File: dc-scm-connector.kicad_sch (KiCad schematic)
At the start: 10 parts, among them J19 Socket_Amphenol_ME10168134011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

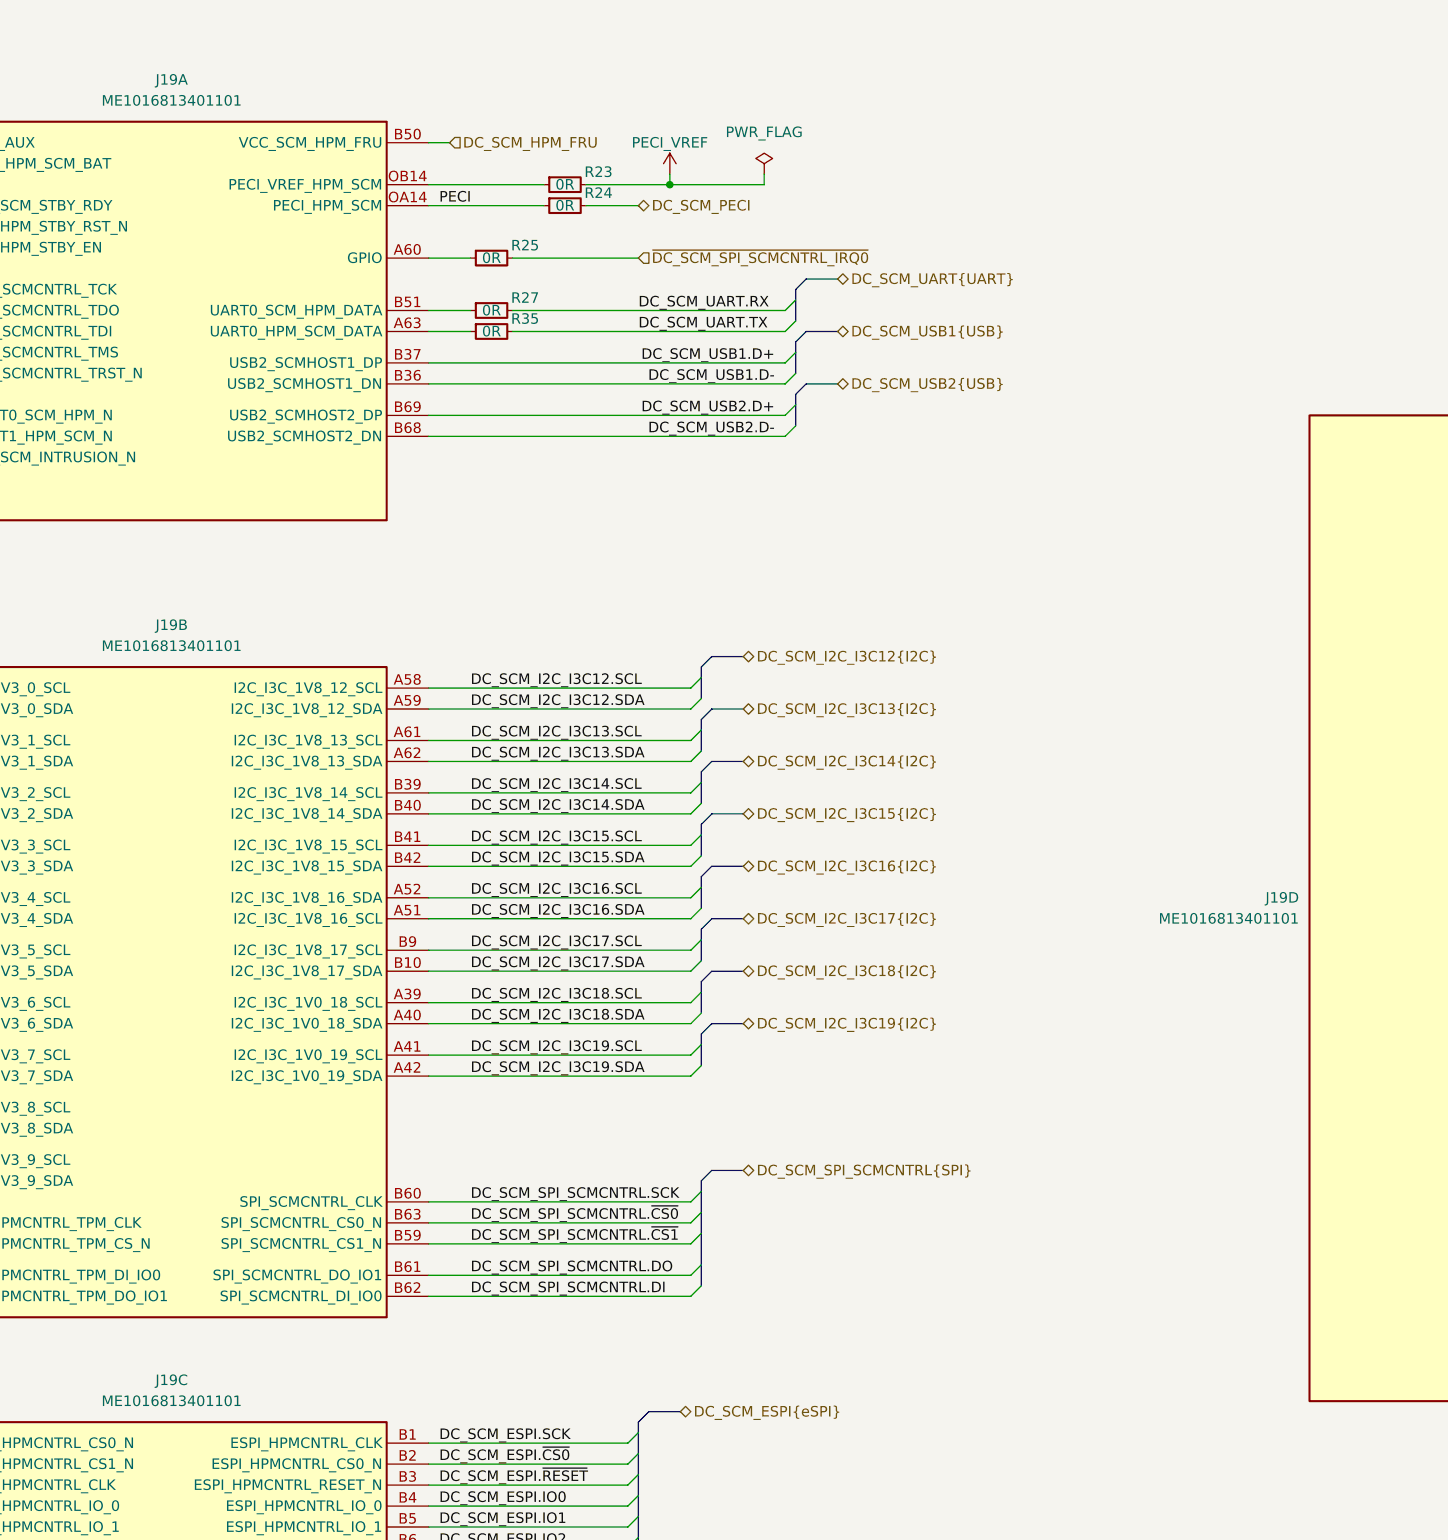
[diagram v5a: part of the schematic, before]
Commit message: [#92504] Update Annotation for connectors
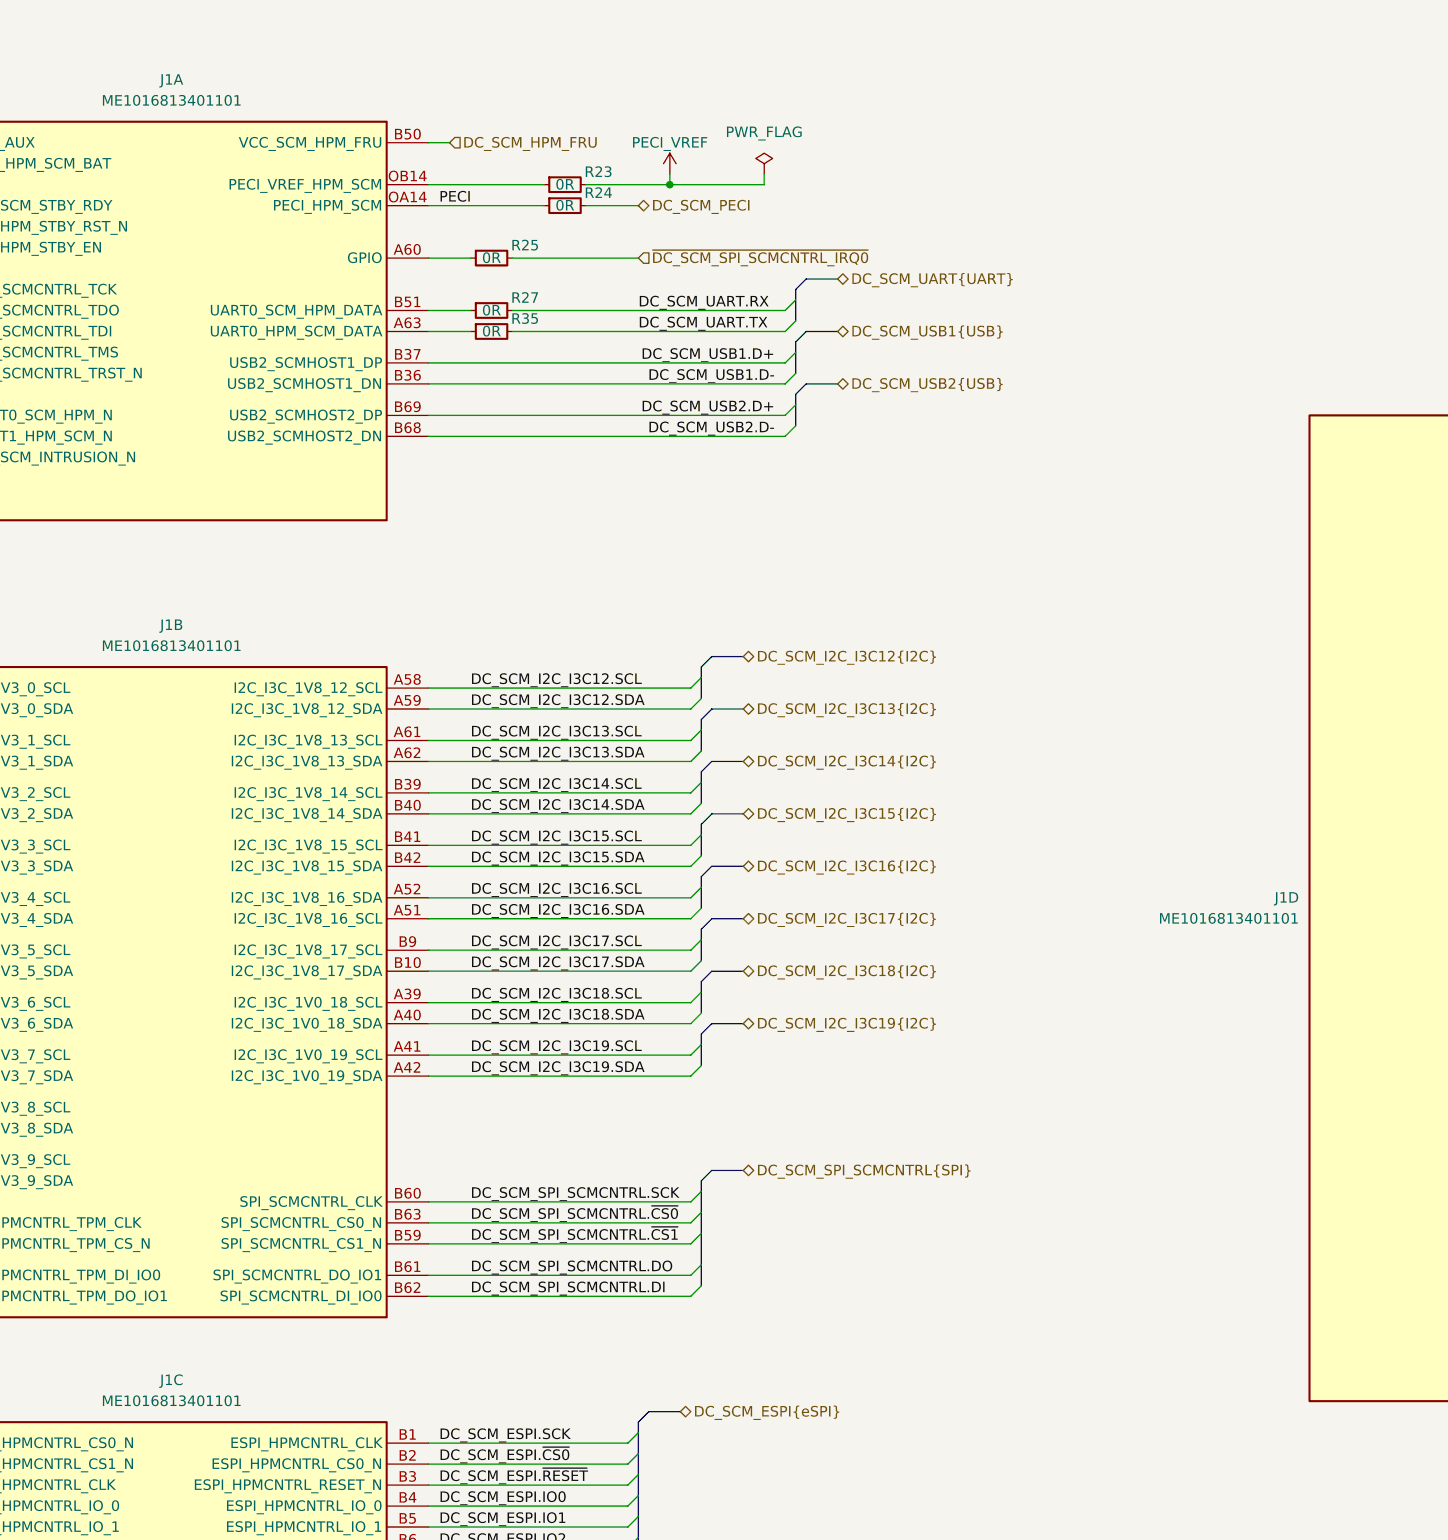
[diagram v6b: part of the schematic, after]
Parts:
- renumbered J19 to J1
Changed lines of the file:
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@@
 		(dnp no)
 		(fields_autoplaced yes)
-		(property "Reference" "J19"
+		(property "Reference" "J1"
 			(at 116.205 194.31 0)
 			(effects
@@
 			(project ""
 				(path "/5d67ef28-5805-4f87-b722-2926dabf7f6e/bae8cef5-57a9-4ec0-acbe-6dac48c5cdf5"
-					(reference "J19")
+					(reference "J1")
 					(unit 3)
 				)
@@
 		(on_board yes)
 		(dnp no)
-		(property "Reference" "J19"
+		(property "Reference" "J1"
 			(at 252.73 135.89 0)
 			(effects
@@
 			(project ""
 				(path "/5d67ef28-5805-4f87-b722-2926dabf7f6e/bae8cef5-57a9-4ec0-acbe-6dac48c5cdf5"
-					(reference "J19")
+					(reference "J1")
 					(unit 4)
 				)
@@
 		(dnp no)
 		(fields_autoplaced yes)
-		(property "Reference" "J19"
+		(property "Reference" "J1"
 			(at 116.205 36.83 0)
 			(effects
@@
 			(project ""
 				(path "/5d67ef28-5805-4f87-b722-2926dabf7f6e/bae8cef5-57a9-4ec0-acbe-6dac48c5cdf5"
-					(reference "J19")
+					(reference "J1")
 					(unit 1)
 				)
@@
 		(dnp no)
 		(fields_autoplaced yes)
-		(property "Reference" "J19"
+		(property "Reference" "J1"
 			(at 116.205 102.87 0)
 			(effects
@@
 			(project ""
 				(path "/5d67ef28-5805-4f87-b722-2926dabf7f6e/bae8cef5-57a9-4ec0-acbe-6dac48c5cdf5"
-					(reference "J19")
+					(reference "J1")
 					(unit 2)
 				)
